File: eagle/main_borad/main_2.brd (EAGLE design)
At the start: 50.8 x 45.7 mm, 35 parts, among them Q2 BSS123, Q3 BSS123, Q5 BSS123, Q6 BSS123, U1 XMEGA-A4TQFP

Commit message: main_board, ver 3.0
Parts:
- removed JP9: (no value), pinhead:1X02
- moved R7 19.5 mm to (44.1, 26.4), flipped to the top, turned to 90 degrees
- moved JP10 17.0 mm to (30.5, 40.6), turned to 180 degrees
- moved Q5 14.5 mm to (40.6, 26.7), flipped to the top, turned to 0 degrees
- moved R4 11.9 mm to (7.62, 10.2), turned to 270 degrees
- moved JP3 11.5 mm to (13.3, 5.71), turned to 180 degrees
- moved C3 10.9 mm to (29.5, 25.7)
- moved U1 10.4 mm to (21.0, 28.9)
- moved Q6 9.55 mm to (36.5, 26.7), flipped to the top, turned to 0 degrees
- moved R9 9.21 mm to (41.0, 31.4), flipped to the top, turned to 180 degrees
- moved JP2 9.09 mm to (7.94, 31.1)
- moved JP8 8.90 mm to (34.9, 21.0), turned to 180 degrees
- moved Q3 7.99 mm to (10.8, 10.2), turned to 0 degrees
- moved R3 7.31 mm to (19.1, 10.2), turned to 90 degrees
- moved JP4 7.25 mm to (13.3, 18.4), turned to 180 degrees
- moved C2 7.20 mm to (20.3, 14.0), turned to 0 degrees
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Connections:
- net GND: no longer JP9.1
- net VCC: no longer JP9.2
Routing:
- net GND: track 0.00 -> 16.7 mm, vias 0 -> 3
- net SCL1: track 20.0 -> 36.7 mm
- net SDA1: track 35.0 -> 47.5 mm
- net N$19: track 23.0 -> 11.3 mm
- net N$24: track 4.83 -> 15.7 mm
- net N$23: track 6.65 -> 17.4 mm
- net N$22: track 9.95 -> 20.6 mm
- net N$21: track 13.0 -> 23.6 mm
- net SCL0: track 35.6 -> 25.4 mm
- net N$11: track 9.98 -> 17.8 mm
- net N$2: track 8.80 -> 16.5 mm
- net N$17: track 14.0 -> 6.56 mm
- net N$16: track 14.7 -> 8.21 mm
- net N$7: track 13.6 -> 7.53 mm
- net N$4: track 15.4 -> 10.2 mm
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- removed copper zone on layer 16, net N$3
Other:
- board size 50.8 x 45.7 mm -> 49.5 x 46 mm

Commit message: PCB ver. 4.0
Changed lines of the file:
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@@
 <wire x1="0" y1="46.0375" x2="0" y2="0" width="0" layer="20"/>
 <hole x="3.175" y="42.545" drill="3.2"/>
-<hole x="46.99" y="42.545" drill="3.2"/>
+<hole x="46.6725" y="42.545" drill="3.2"/>
 <hole x="46.6725" y="3.175" drill="3.2"/>
 <hole x="3.175" y="3.175" drill="3.2"/>

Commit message: PCB layout 6.0
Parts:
- JP10: device pinhead:1X04 -> pinhead:1X05
- JP8: device pinhead:1X02 -> pinhead:1X03
- moved JP6 11.3 mm to (23.8, 49.8)
- moved JP8 10.9 mm to (41.3, 29.8)
- moved JP5 10.9 mm to (42.9, 45.4)
- moved JP2 10.7 mm to (14.0, 40.0)
- moved C3 10.7 mm to (35.6, 34.6)
- moved C4 10.7 mm to (33.0, 14.6)
- moved JP1 10.7 mm to (30.8, 18.7)
- moved Q2 10.7 mm to (21.3, 19.1)
- moved Q3 10.7 mm to (16.8, 19.1)
- moved R4 10.7 mm to (13.7, 19.1)
- moved U1 10.7 mm to (27.0, 37.8)
- moved C2 10.7 mm to (26.4, 22.9)
- moved JP3 10.7 mm to (19.4, 14.6)
- moved JP4 10.7 mm to (19.4, 27.3)
- moved JP7 10.7 mm to (28.3, 14.6)
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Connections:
- net VCC: now also JP10.5, JP8.3
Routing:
- net VCC: track 150.3 -> 165.4 mm
- net SDA0: track 50.3 -> 54.4 mm
- net SCL0: track 25.4 -> 28.2 mm
- net N$19: track 11.3 -> 14.0 mm
- net GND: track 16.7 -> 14.6 mm, vias 3 -> 5
- net N$20: track 12.0 -> 10.4 mm
- net SCL1: track 36.7 -> 37.4 mm
- net N$16: track 8.21 -> 8.84 mm
- net N$4: track 10.2 -> 10.9 mm
- net N$17: track 6.56 -> 7.19 mm
- net SDA1: track 47.5 -> 48.1 mm
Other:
- board size 49.5 x 46 mm -> 63.4 x 63.4 mm
- board text added: "5v"
- board text added: "gnd"
- board text added: "miso"
- board text added: "mosi"
- board text added: "pdi-clk"
- board text added: "pdi-data"
- board text added: "rst"
- board text added: "rxd0"
- board text added: "sck/17"
- board text added: "sck0"
- board text added: "scl0"
- board text added: "scl1"
- board text added: "sda0"
- board text added: "sda1"
- board text added: "ss"
- board text added: "txd0"
- board text added: "vcc"
- board text added: "xck0"

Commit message: Bugs
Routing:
- net GND: track 14.6 -> 11.5 mm
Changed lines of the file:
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@@
 <layers>
 <layer number="1" name="Top" color="4" fill="1" visible="yes" active="yes"/>
-<layer number="16" name="Bottom" color="1" fill="1" visible="yes" active="yes"/>
+<layer number="16" name="Bottom" color="1" fill="1" visible="no" active="yes"/>
 <layer number="17" name="Pads" color="2" fill="1" visible="yes" active="yes"/>
 <layer number="18" name="Vias" color="2" fill="1" visible="yes" active="yes"/>
@@
 <hole x="55" y="5" drill="3.2"/>
 <hole x="5" y="5" drill="3.2"/>
-<text x="8.5725" y="46.99" size="1.016" layer="1">xck0</text>
-<text x="8.5725" y="44.45" size="1.016" layer="1">rxd0</text>
-<text x="8.5725" y="41.91" size="1.016" layer="1">txd0</text>
-<text x="8.5725" y="39.6875" size="1.016" layer="1">ss</text>
-<text x="8.5725" y="36.83" size="1.016" layer="1">mosi</text>
-<text x="8.5725" y="34.29" size="1.016" layer="1">miso</text>
-<text x="8.5725" y="31.75" size="1.016" layer="1">sck0</text>
-<text x="23.495" y="8.255" size="1.016" layer="1" rot="R90">gnd</text>
-<text x="21.2725" y="7.9375" size="1.016" layer="1" rot="R90">sda1</text>
-<text x="19.05" y="8.255" size="1.016" layer="1" rot="R90">scl1</text>
-<text x="16.8275" y="8.255" size="1.016" layer="1" rot="R90">vcc</text>
-<text x="28.575" y="4.445" size="1.016" layer="1" rot="R90">rst</text>
-<text x="31.4325" y="7.3025" size="1.016" layer="1" rot="R90">pdi-clk</text>
-<text x="28.575" y="7.3025" size="1.016" layer="1" rot="R90">pdi-data</text>
-<text x="19.05" y="4.7625" size="1.016" layer="1" rot="R90">5v</text>
-<text x="16.8275" y="4.7625" size="1.016" layer="1" rot="R90">scl1</text>
-<text x="25.7175" y="54.9275" size="1.016" layer="1" rot="R270">mosi</text>
-<text x="23.1775" y="54.9275" size="1.016" layer="1" rot="R270">miso</text>
-<text x="20.6375" y="55.88" size="1.016" layer="1" rot="R270">sck/17</text>
-<text x="40.64" y="52.3875" size="1.016" layer="1" rot="R90">gnd</text>
-<text x="38.1" y="52.705" size="1.016" layer="1" rot="R90">sda0</text>
-<text x="35.56" y="52.705" size="1.016" layer="1" rot="R90">scl0</text>
-<text x="33.02" y="52.705" size="1.016" layer="1" rot="R90">vcc</text>
-<text x="50.4825" y="8.5725" size="1.016" layer="1" rot="R90">gnd</text>
-<text x="48.26" y="8.5725" size="1.016" layer="1" rot="R90">sda0</text>
-<text x="46.0375" y="8.5725" size="1.016" layer="1" rot="R90">5v</text>
-<text x="43.815" y="8.5725" size="1.016" layer="1" rot="R90">scl0</text>
-<text x="46.0375" y="5.08" size="1.016" layer="1" rot="R90">gnd</text>
-<text x="43.815" y="5.08" size="1.016" layer="1" rot="R90">vcc</text>
+<text x="8.5725" y="46.99" size="1.016" layer="51">xck0</text>
+<text x="8.5725" y="44.45" size="1.016" layer="51">rxd0</text>
+<text x="8.5725" y="41.91" size="1.016" layer="51">txd0</text>
+<text x="8.5725" y="39.6875" size="1.016" layer="51">ss</text>
+<text x="8.5725" y="36.83" size="1.016" layer="51">mosi</text>
+<text x="8.5725" y="34.29" size="1.016" layer="51">miso</text>
+<text x="8.5725" y="31.75" size="1.016" layer="51">sck0</text>
+<text x="23.495" y="8.255" size="1.016" layer="51" rot="R90">gnd</text>
+<text x="21.2725" y="7.9375" size="1.016" layer="51" rot="R90">sda1</text>
+<text x="19.05" y="8.255" size="1.016" layer="51" rot="R90">scl1</text>
+<text x="16.8275" y="8.255" size="1.016" layer="51" rot="R90">vcc</text>
+<text x="28.575" y="4.445" size="1.016" layer="51" rot="R90">rst</text>
+<text x="31.4325" y="7.3025" size="1.016" layer="51" rot="R90">pdi-clk</text>
+<text x="28.575" y="7.3025" size="1.016" layer="51" rot="R90">pdi-data</text>
+<text x="19.05" y="4.7625" size="1.016" layer="51" rot="R90">5v</text>
+<text x="16.8275" y="4.7625" size="1.016" layer="51" rot="R90">scl1</text>
+<text x="25.7175" y="54.9275" size="1.016" layer="51" rot="R270">mosi</text>
+<text x="23.1775" y="54.9275" size="1.016" layer="51" rot="R270">miso</text>
+<text x="20.6375" y="55.88" size="1.016" layer="51" rot="R270">sck/17</text>
+<text x="40.64" y="52.3875" size="1.016" layer="51" rot="R90">gnd</text>
+<text x="38.1" y="52.705" size="1.016" layer="51" rot="R90">sda0</text>
+<text x="35.56" y="52.705" size="1.016" layer="51" rot="R90">scl0</text>
+<text x="33.02" y="52.705" size="1.016" layer="51" rot="R90">vcc</text>
+<text x="50.4825" y="8.5725" size="1.016" layer="51" rot="R90">gnd</text>
+<text x="48.26" y="8.5725" size="1.016" layer="51" rot="R90">sda0</text>
+<text x="46.0375" y="8.5725" size="1.016" layer="51" rot="R90">5v</text>
+<text x="43.815" y="8.5725" size="1.016" layer="51" rot="R90">scl0</text>
+<text x="46.0375" y="5.08" size="1.016" layer="51" rot="R90">gnd</text>
+<text x="43.815" y="5.08" size="1.016" layer="51" rot="R90">vcc</text>
 <wire x1="-1.705" y1="33" x2="-1.705" y2="61.705" width="3.81" layer="46"/>
 <wire x1="-1.705" y1="61.705" x2="61.705" y2="61.705" width="3.81" layer="46"/>
@@
 <attribute name="VALUE" x="12.3825" y="15.875" size="1.27" layer="27"/>
 </element>
-<element name="Q5" library="transistor-small-signal" package="SOT23" value="BSS123" x="46.6725" y="35.56"/>
+<element name="Q5" library="transistor-small-signal" package="SOT23" value="BSS123" x="46.6725" y="35.56" smashed="yes">
+<attribute name="NAME" x="48.5775" y="36.195" size="1.27" layer="25"/>
+<attribute name="VALUE" x="44.7675" y="32.385" size="1.27" layer="27"/>
+</element>
 <element name="Q6" library="transistor-small-signal" package="SOT23" value="BSS123" x="42.545" y="35.56"/>
 <element name="R1" library="eagle-ltspice" package="R0805" value="220" x="47.625" y="21.2725" rot="R270">
@@
 <wire x1="41.275" y1="29.845" x2="38.735" y2="29.845" width="0.8128" layer="1"/>
 <contactref element="JP10" pad="5"/>
-<wire x1="32.7025" y1="49.8475" x2="30.1625" y2="49.8475" width="0.8128" layer="1"/>
 <wire x1="18.627290625" y1="12.7" x2="15.875" y2="12.7" width="0.3048" layer="1"/>
 <wire x1="15.875" y1="12.7" x2="15.5575" y2="13.0175" width="0.3048" layer="1"/>
@@
 <wire x1="15.5575" y1="16.51" x2="15.8775" y2="16.83" width="0.3048" layer="1"/>
 <wire x1="15.8775" y1="16.83" x2="15.8775" y2="17.95" width="0.3048" layer="1"/>
+<wire x1="32.7025" y1="49.8475" x2="30.1625" y2="49.8475" width="0.8128" layer="1"/>
 <wire x1="15.5575" y1="13.0175" x2="15.5575" y2="14.605" width="0" layer="19" extent="1-1"/>
 </signal>
@@
 <via x="27.305" y="24.765" extent="1-16" drill="0.6"/>
 <wire x1="27.305" y1="24.765" x2="27.305" y2="26.035" width="0.3048" layer="16"/>
-<wire x1="19.685" y1="30.1625" x2="18.415" y2="30.1625" width="0.3048" layer="16"/>
-<wire x1="19.685" y1="30.1625" x2="19.685" y2="29.21" width="0.3048" layer="16"/>
 <wire x1="19.685" y1="30.1625" x2="19.685" y2="31.115" width="0.3048" layer="16"/>
 <wire x1="27.305" y1="24.765" x2="28.2575" y2="24.765" width="0.3048" layer="16"/>
 <wire x1="27.305" y1="24.765" x2="26.3525" y2="24.765" width="0.3048" layer="16"/>
-<wire x1="19.685" y1="30.1625" x2="20.6375" y2="30.1625" width="0.3048" layer="16"/>
 <polygon width="0.4064" layer="16">
 <vertex x="-4.7625" y="-6.6675"/>
@@
 <via x="19.685" y="30.1625" extent="1-16" drill="0.6"/>
 <via x="27.305" y="24.765" extent="1-16" drill="0.6"/>
-<wire x1="21.1875" y1="36.1825" x2="21.1875" y2="34.5825" width="0" layer="19" extent="1-1"/>
 </signal>
 <signal name="N$1">

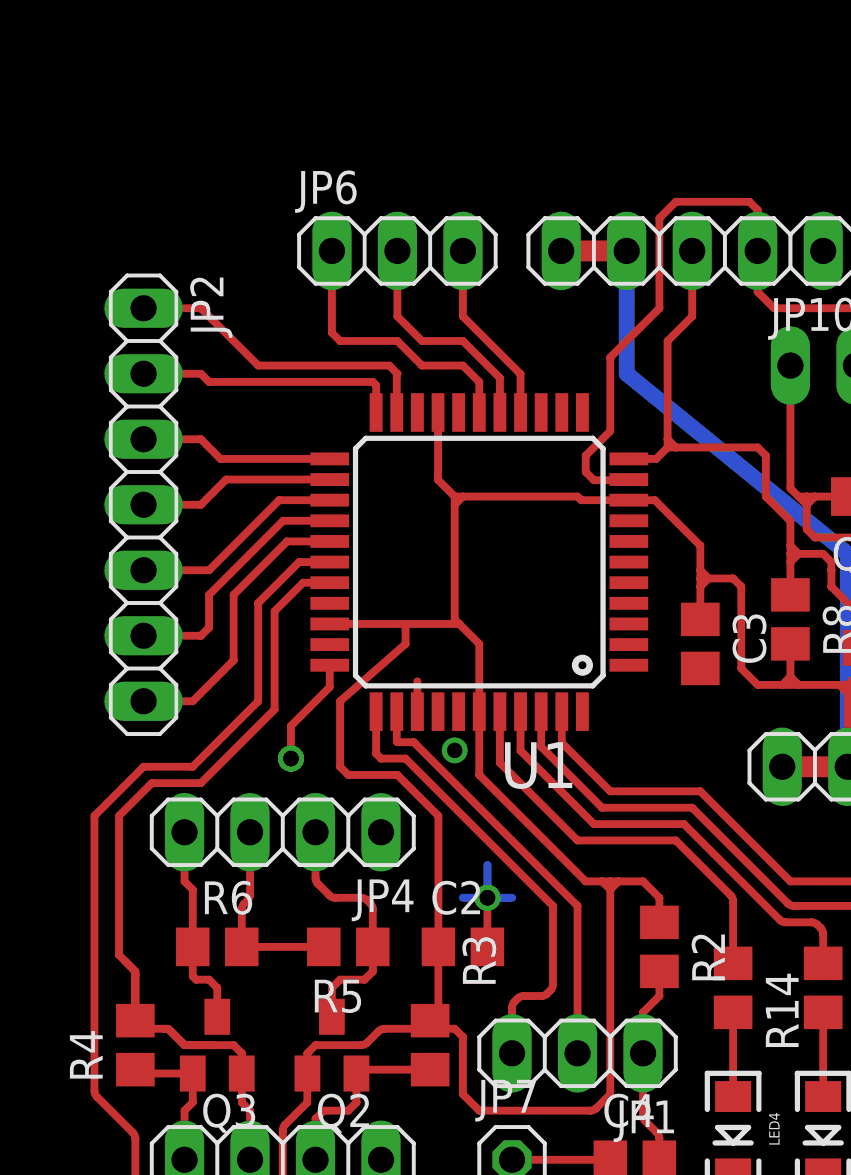
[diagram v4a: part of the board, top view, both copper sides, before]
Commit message: motor_drivers updated
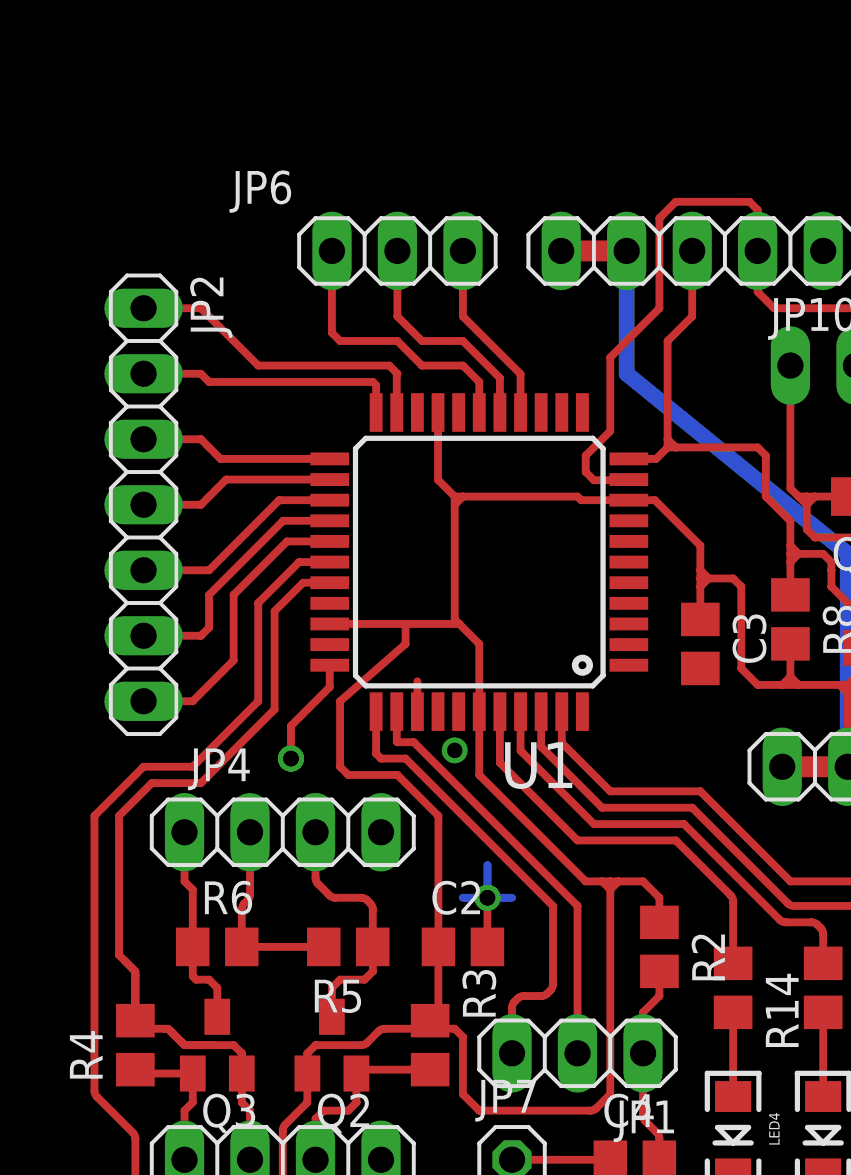
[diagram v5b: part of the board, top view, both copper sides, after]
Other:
- board text added: "miso/16"
- board text added: "miso/26"
- board text added: "mosi/15"
- board text added: "mosi/25"
- board text added: "rxd0/22"
- board text added: "sck/27"
- board text added: "scl0/11"
- board text added: "sda0/10"
- board text added: "ss/24"
- board text added: "txd0/23"
- board text added: "xck0/21"
- board text removed: "miso"
- board text removed: "mosi"
- board text removed: "rxd0"
- board text removed: "sck0"
- board text removed: "ss"
- board text removed: "txd0"
- board text removed: "xck0"
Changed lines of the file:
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@@
 <setting verticaltext="up"/>
 </settings>
-<grid distance="1.27" unitdist="mm" unit="mm" style="lines" multiple="1" display="no" altdistance="0.025" altunitdist="inch" altunit="inch"/>
+<grid distance="0.0125" unitdist="inch" unit="inch" style="lines" multiple="1" display="no" altdistance="0.025" altunitdist="inch" altunit="inch"/>
 <layers>
 <layer number="1" name="Top" color="4" fill="1" visible="yes" active="yes"/>
-<layer number="16" name="Bottom" color="1" fill="1" visible="no" active="yes"/>
+<layer number="16" name="Bottom" color="1" fill="1" visible="yes" active="yes"/>
 <layer number="17" name="Pads" color="2" fill="1" visible="yes" active="yes"/>
 <layer number="18" name="Vias" color="2" fill="1" visible="yes" active="yes"/>
@@
 <hole x="55" y="5" drill="3.2"/>
 <hole x="5" y="5" drill="3.2"/>
-<text x="8.5725" y="46.99" size="1.016" layer="51">xck0</text>
-<text x="8.5725" y="44.45" size="1.016" layer="51">rxd0</text>
-<text x="8.5725" y="41.91" size="1.016" layer="51">txd0</text>
-<text x="8.5725" y="39.6875" size="1.016" layer="51">ss</text>
-<text x="8.5725" y="36.83" size="1.016" layer="51">mosi</text>
-<text x="8.5725" y="34.29" size="1.016" layer="51">miso</text>
-<text x="8.5725" y="31.75" size="1.016" layer="51">sck0</text>
+<text x="7.3025" y="46.99" size="1.016" layer="51">xck0/21</text>
+<text x="7.3025" y="44.45" size="1.016" layer="51">rxd0/22</text>
+<text x="7.3025" y="41.91" size="1.016" layer="51">txd0/23</text>
+<text x="7.3025" y="39.6875" size="1.016" layer="51">ss/24</text>
+<text x="7.3025" y="36.83" size="1.016" layer="51">mosi/25</text>
+<text x="7.3025" y="34.29" size="1.016" layer="51">miso/26</text>
+<text x="7.3025" y="31.75" size="1.016" layer="51">sck/27</text>
 <text x="23.495" y="8.255" size="1.016" layer="51" rot="R90">gnd</text>
 <text x="21.2725" y="7.9375" size="1.016" layer="51" rot="R90">sda1</text>
@@
 <text x="19.05" y="4.7625" size="1.016" layer="51" rot="R90">5v</text>
 <text x="16.8275" y="4.7625" size="1.016" layer="51" rot="R90">scl1</text>
-<text x="25.7175" y="54.9275" size="1.016" layer="51" rot="R270">mosi</text>
-<text x="23.1775" y="54.9275" size="1.016" layer="51" rot="R270">miso</text>
-<text x="20.6375" y="55.88" size="1.016" layer="51" rot="R270">sck/17</text>
+<text x="25.7175" y="57.4675" size="1.016" layer="51" rot="R270">mosi/15</text>
+<text x="23.1775" y="57.4675" size="1.016" layer="51" rot="R270">miso/16</text>
+<text x="20.6375" y="57.15" size="1.016" layer="51" rot="R270">sck/17</text>
 <text x="40.64" y="52.3875" size="1.016" layer="51" rot="R90">gnd</text>
-<text x="38.1" y="52.705" size="1.016" layer="51" rot="R90">sda0</text>
-<text x="35.56" y="52.705" size="1.016" layer="51" rot="R90">scl0</text>
+<text x="38.1" y="52.705" size="1.016" layer="51" rot="R90">sda0/10</text>
+<text x="35.56" y="52.705" size="1.016" layer="51" rot="R90">scl0/11</text>
 <text x="33.02" y="52.705" size="1.016" layer="51" rot="R90">vcc</text>
 <text x="50.4825" y="8.5725" size="1.016" layer="51" rot="R90">gnd</text>
@@
 <dimension x1="60" y1="0" x2="60" y2="60" x3="83.82" y3="30" textsize="1.27" layer="46"/>
 <dimension x1="0" y1="0" x2="60" y2="0" x3="30" y3="-20.32" textsize="1.27" layer="46"/>
+<text x="21.2725" y="4.1275" size="1.016" layer="51" rot="R90">sda1</text>
+<text x="23.495" y="4.7625" size="1.016" layer="51" rot="R90">gnd</text>
 </plain>
 <attributes>
@@
 <element name="JP2" library="pinhead" package="1X07" value="" x="13.97" y="40.005" rot="R270"/>
 <element name="JP3" library="pinhead" package="1X04" value="" x="19.3675" y="14.605" rot="R180"/>
-<element name="JP4" library="pinhead" package="1X04" value="" x="19.3675" y="27.305" rot="R180"/>
+<element name="JP4" library="pinhead" package="1X04" value="" x="19.3675" y="27.305" smashed="yes" rot="R180">
+<attribute name="NAME" x="18.1737" y="30.5562" size="1.27" layer="25" ratio="10" rot="R180"/>
+<attribute name="VALUE" x="24.4475" y="30.48" size="1.27" layer="27" rot="R180"/>
+</element>
 <element name="JP5" library="pinhead" package="1X04" value="" x="42.8625" y="45.4025" smashed="yes" rot="MR0">
 <attribute name="NAME" x="51.1937" y="45.6438" size="1.27" layer="26" ratio="10" rot="MR0"/>
 <attribute name="VALUE" x="47.9425" y="42.2275" size="1.27" layer="28" rot="MR0"/>
 </element>
-<element name="JP6" library="pinhead" package="1X03" value="" x="23.8125" y="49.8475"/>
+<element name="JP6" library="pinhead" package="1X03" value="" x="23.8125" y="49.8475" smashed="yes">
+<attribute name="NAME" x="17.3863" y="51.6763" size="1.27" layer="25" ratio="10"/>
+<attribute name="VALUE" x="20.0025" y="46.6725" size="1.27" layer="27"/>
+</element>
 <element name="JP7" library="pinhead" package="1X01" value="" x="28.2575" y="14.605"/>
 <element name="LED2" library="SparkFun-LED" package="LED-1206" value="" x="44.1325" y="15.5575" rot="R270"/>
@@
 <attribute name="SPICEMODEL" value="NONE" x="25.0825" y="19.05" size="1.778" layer="27" rot="R90" display="off"/>
 <attribute name="SPICEPREFIX" value="R" x="25.0825" y="19.05" size="1.778" layer="27" rot="R90" display="off"/>
-<attribute name="NAME" x="27.6225" y="21.2725" size="1.27" layer="25" rot="R90"/>
+<attribute name="NAME" x="27.6225" y="20.0025" size="1.27" layer="25" rot="R90"/>
 <attribute name="VALUE" x="27.6225" y="18.415" size="1.27" layer="27" rot="R90"/>
 </element>
@@
 <wire x1="43.495" y1="34.46" x2="43.495" y2="34.9275" width="0.3048" layer="1"/>
 <wire x1="43.18" y1="35.56" x2="41.91" y2="35.56" width="0.3048" layer="1"/>
-<contactref element="JP10" pad="3"/>
 <wire x1="39.055" y1="36.8275" x2="39.0525" y2="36.83" width="0.3048" layer="1"/>
 <wire x1="39.0525" y1="36.83" x2="39.0525" y2="37.7825" width="0.3048" layer="1"/>
@@
 <wire x1="34.29" y1="42.545" x2="34.29" y2="46.355" width="0.3048" layer="1"/>
 <wire x1="34.29" y1="46.355" x2="35.2425" y2="47.3075" width="0.3048" layer="1"/>
-<wire x1="35.2425" y1="47.3075" x2="35.2425" y2="49.8475" width="0.3048" layer="1"/>
 <wire x1="40.6425" y1="36.8275" x2="40.6425" y2="37.4625" width="0.3048" layer="1"/>
 <wire x1="40.6425" y1="37.4625" x2="40.64" y2="37.465" width="0.3048" layer="1"/>
@@
 <wire x1="38.1" y1="40.3225" x2="39.0525" y2="39.37" width="0.3048" layer="1"/>
 <wire x1="39.0525" y1="39.37" x2="39.0525" y2="38.4175" width="0.3048" layer="1"/>
+<contactref element="JP10" pad="3"/>
+<wire x1="35.2425" y1="49.8475" x2="35.2425" y2="47.3075" width="0.3048" layer="1"/>
 </signal>
 <signal name="SDA0">
